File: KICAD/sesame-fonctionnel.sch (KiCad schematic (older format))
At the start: 9 parts, among them J1 CXS70-14-C, J2 CXS70-14-C, J3 6095, J4 6095, J5 6095, J6 6095, J7 CXS70-14-C, J8 CXS70-14-C

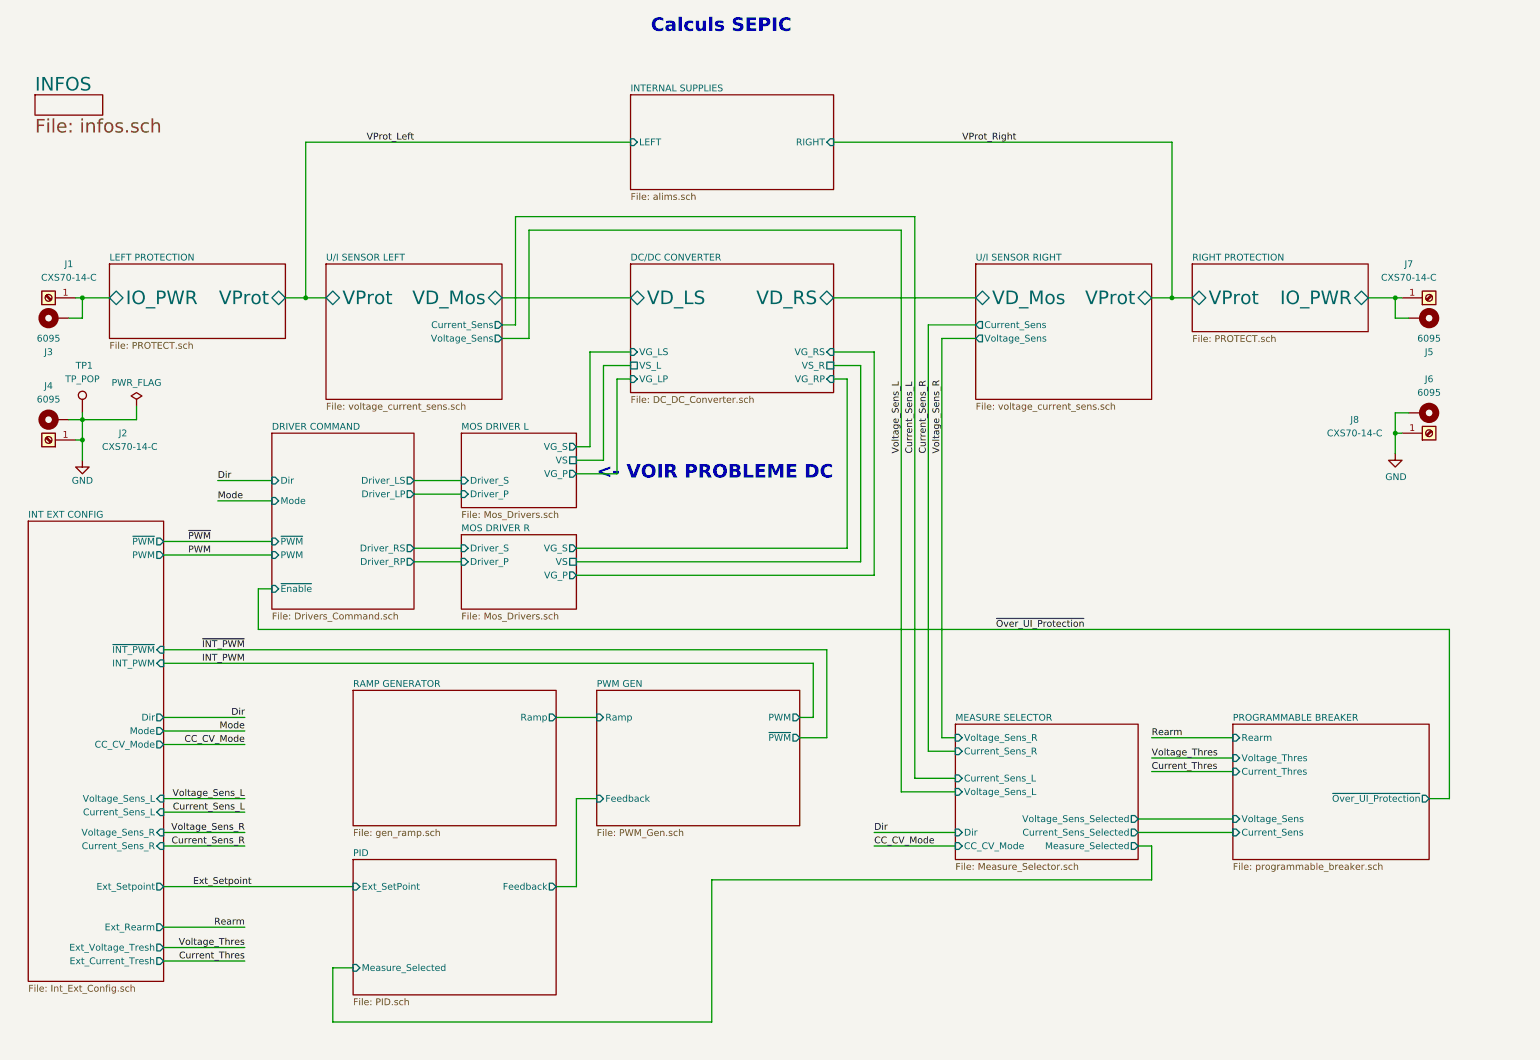
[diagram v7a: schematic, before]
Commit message: edit footprints by jmt
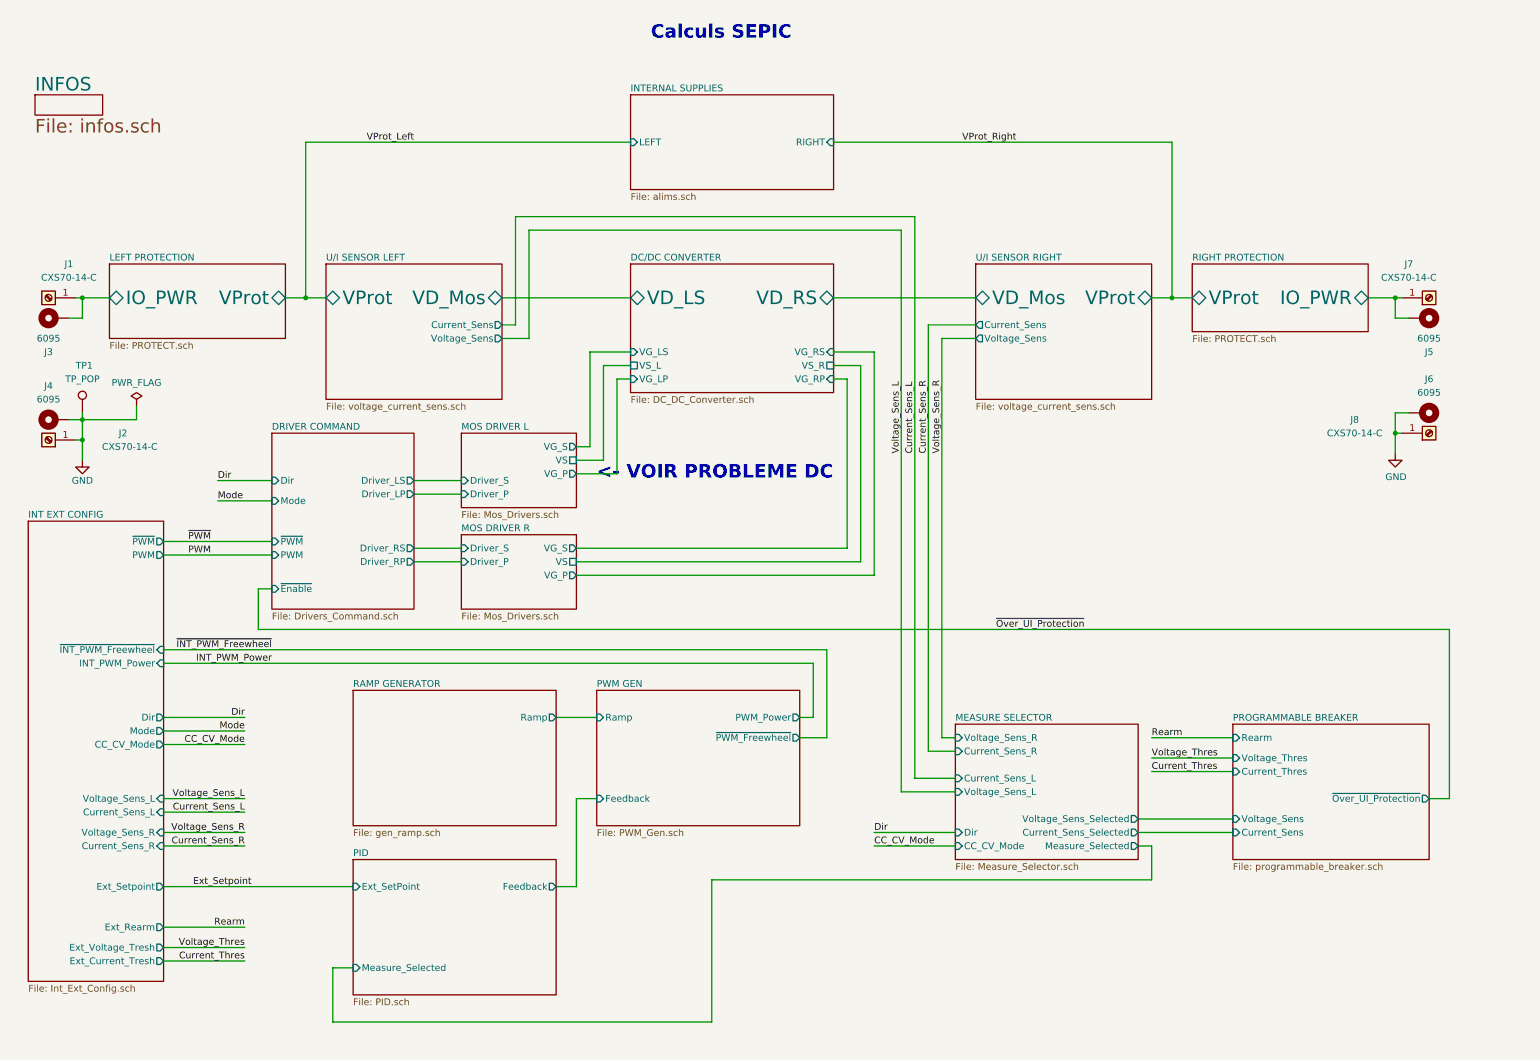
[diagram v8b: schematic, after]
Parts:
- TP1: footprint (none) -> TestPoint:TestPoint_Loop_D1.80mm_Drill1.0mm_Beaded
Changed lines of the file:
@@
 F10 "~Enable" I L 2400 4350 50
 $EndSheet
-Text Label 2200 4900 2    50   ~ 0
-INT_PWM
-Text Label 2200 4800 2    50   ~ 0
-~INT_PWM
+Text Label 2400 4900 2    50   ~ 0
+INT_PWM_Power
+Text Label 2400 4800 2    50   ~ 0
+~INT_PWM_Freewheel
 Wire Wire Line
 	6850 6150 7450 6150
@@
 Text Label 7250 3350 1    50   ~ 0
 Current_Sens_R
-$Sheet
-S 4800 5100 1500 1000
-U 60F1AF26
-F0 "PWM GEN" 50
-F1 "PWM_Gen.sch" 50
-F2 "Ramp" I L 4800 5300 50
-F3 "PWM" O R 6300 5300 50
-F4 "~PWM" O R 6300 5450 50
-F5 "Feedback" I L 4800 5900 50
-$EndSheet
 Wire Wire Line
 	7150 1600 7150 5750
@@
 F6 "Dir" O R 1600 5300 50
 F7 "Mode" O R 1600 5400 50
-F8 "INT_PWM" I R 1600 4900 50
-F9 "~INT_PWM" I R 1600 4800 50
-F10 "PWM" O R 1600 4100 50
-F11 "~PWM" O R 1600 4000 50
-F12 "CC_CV_Mode" O R 1600 5500 50
-F13 "Ext_Setpoint" O R 1600 6550 50
-F14 "Ext_Current_Tresh" O R 1600 7100 50
-F15 "Ext_Voltage_Tresh" O R 1600 7000 50
-F16 "Ext_Rearm" O R 1600 6850 50
+F8 "PWM" O R 1600 4100 50
+F9 "~PWM" O R 1600 4000 50
+F10 "CC_CV_Mode" O R 1600 5500 50
+F11 "Ext_Setpoint" O R 1600 6550 50
+F12 "Ext_Current_Tresh" O R 1600 7100 50
+F13 "Ext_Voltage_Tresh" O R 1600 7000 50
+F14 "Ext_Rearm" O R 1600 6850 50
+F15 "INT_PWM_Power" I R 1600 4900 50
+F16 "~INT_PWM_Freewheel" I R 1600 4800 50
 $EndSheet
 Wire Wire Line
@@
 Text Label 1950 4100 2    50   ~ 0
 PWM
-Text Notes 5200 250  0    100  ~ 20
+Text Notes 5200 300  0    100  ~ 20
 Calculs SEPIC
 $Sheet
@@
 F 0 "TP1" H 950 3400 50  0000 L CNN
 F 1 "TP_POP" H 1000 3300 50  0000 C CNN
-F 2 "" H 1200 3050 50  0001 C CNN
+F 2 "TestPoint:TestPoint_Loop_D1.80mm_Drill1.0mm_Beaded" H 1200 3050 50  0001 C CNN
 F 3 "~" H 1200 3050 50  0001 C CNN
 	1    1000 3050
@@
 Text Notes 4800 3550 0    100  ~ 20
 <- VOIR PROBLEME DC
+$Sheet
+S 4800 5100 1500 1000
+U 60F1AF26
+F0 "PWM GEN" 50
+F1 "PWM_Gen.sch" 50
+F2 "Ramp" I L 4800 5300 50
+F3 "Feedback" I L 4800 5900 50
+F4 "~PWM_Freewheel" O R 6300 5450 50
+F5 "PWM_Power" O R 6300 5300 50
+$EndSheet
 $EndSCHEMATC
